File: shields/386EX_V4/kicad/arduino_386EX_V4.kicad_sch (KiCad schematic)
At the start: 48 parts, among them J1 Conn_01x02_Pin, J2 JTAG, J3 Conn_01x04_Pin, J4 Conn_01x04_Pin, J5 Conn_01x04_Pin, J6 SERIAL0, J9 WP Jumper, U1 AT24CS01-STUM, U11 I386EX_PQFP, U2 ULN2003A, U3 SN74LV14A

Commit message: Fixed oversight of I2C SDA and SCK pull-up resistors; rearranged EEPROM IC to accommodate.
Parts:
- added R14, R15: 3.3 K Ohm, Resistor_SMD:R_0603_1608Metric_Pad0.98x0.95mm_HandSolder, symbol Device:R
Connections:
- net +3.3VP: now also R14.2, R15.2
- net SCL: now also R15.1
- net SDA: now also R14.1
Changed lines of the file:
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@@
 	)
 	(junction
+		(at 300.99 143.51)
+		(diameter 0)
+		(color 0 0 0 0)
+	)
+	(junction
 		(at 386.08 45.72)
 		(diameter 0)
@@
 	)
 	(junction
+		(at 304.8 143.51)
+		(diameter 0)
+		(color 0 0 0 0)
+	)
+	(junction
 		(at 320.04 177.8)
 		(diameter 0)
@@
 	)
 	(junction
+		(at 304.8 158.75)
+		(diameter 0)
+		(color 0 0 0 0)
+	)
+	(junction
 		(at 257.81 256.54)
 		(diameter 0)
@@
 	)
 	(junction
+		(at 300.99 156.21)
+		(diameter 0)
+		(color 0 0 0 0)
+	)
+	(junction
 		(at 257.81 259.08)
 		(diameter 0)
@@
 	(wire
 		(pts
+			(xy 304.8 143.51) (xy 304.8 146.05)
+		)
+		(stroke
+			(width 0)
+			(type default)
+		)
+	)
+	(wire
+		(pts
 			(xy 201.93 287.02) (xy 201.93 294.64)
 		)
@@
 	(wire
 		(pts
-			(xy 287.02 143.51) (xy 320.04 143.51)
+			(xy 287.02 143.51) (xy 300.99 143.51)
 		)
 		(stroke
@@
 	(wire
 		(pts
+			(xy 304.8 153.67) (xy 304.8 158.75)
+		)
+		(stroke
+			(width 0)
+			(type default)
+		)
+	)
+	(wire
+		(pts
 			(xy 95.25 68.58) (xy 100.33 68.58)
 		)
@@
 	(wire
 		(pts
+			(xy 304.8 143.51) (xy 320.04 143.51)
+		)
+		(stroke
+			(width 0)
+			(type default)
+		)
+	)
+	(wire
+		(pts
 			(xy 63.5 233.68) (xy 63.5 241.3)
 		)
@@
 	(wire
 		(pts
+			(xy 300.99 153.67) (xy 300.99 156.21)
+		)
+		(stroke
+			(width 0)
+			(type default)
+		)
+	)
+	(wire
+		(pts
 			(xy 317.5 165.1) (xy 317.5 161.29)
 		)
@@
 	(wire
 		(pts
+			(xy 300.99 143.51) (xy 304.8 143.51)
+		)
+		(stroke
+			(width 0)
+			(type default)
+		)
+	)
+	(wire
+		(pts
 			(xy 100.33 119.38) (xy 95.25 119.38)
 		)
@@
 	(wire
 		(pts
+			(xy 300.99 156.21) (xy 336.55 156.21)
+		)
+		(stroke
+			(width 0)
+			(type default)
+		)
+	)
+	(wire
+		(pts
 			(xy 50.8 323.85) (xy 50.8 332.74)
 		)
@@
 	(wire
 		(pts
-			(xy 297.18 156.21) (xy 336.55 156.21)
+			(xy 297.18 156.21) (xy 300.99 156.21)
 		)
 		(stroke
@@
 	(wire
 		(pts
-			(xy 297.18 158.75) (xy 336.55 158.75)
+			(xy 297.18 158.75) (xy 304.8 158.75)
 		)
 		(stroke
@@
 	(wire
 		(pts
+			(xy 300.99 143.51) (xy 300.99 146.05)
+		)
+		(stroke
+			(width 0)
+			(type default)
+		)
+	)
+	(wire
+		(pts
 			(xy 95.25 214.63) (xy 95.25 220.98)
 		)
@@
 	(wire
 		(pts
+			(xy 304.8 158.75) (xy 336.55 158.75)
+		)
+		(stroke
+			(width 0)
+			(type default)
+		)
+	)
+	(wire
+		(pts
 			(xy 346.71 40.64) (xy 356.87 40.64)
 		)
@@
 	)
 	(symbol
+		(lib_id "Device:R")
+		(at 304.8 149.86 180)
+		(unit 1)
+		(exclude_from_sim no)
+		(in_bom yes)
+		(on_board yes)
+		(dnp no)
+		(property "Reference" "R15"
+			(at 307.34 148.5899 0)
+			(effects
+				(font
+					(size 1.27 1.27)
+				)
+				(justify right)
+			)
+		)
+		(property "Value" "3.3 K Ohm"
+			(at 307.34 151.1299 0)
+			(effects
+				(font
+					(size 1.27 1.27)
+				)
+				(justify right)
+			)
+		)
+		(property "Footprint" "Resistor_SMD:R_0603_1608Metric_Pad0.98x0.95mm_HandSolder"
+			(at 306.578 149.86 90)
+			(effects
+				(font
+					(size 1.27 1.27)
+				)
+				(hide yes)
+			)
+		)
+		(property "Datasheet" "~"
+			(at 304.8 149.86 0)
+			(effects
+				(font
+					(size 1.27 1.27)
+				)
+				(hide yes)
+			)
+		)
+		(property "Description" "Resistor"
+			(at 304.8 149.86 0)
+			(effects
+				(font
+					(size 1.27 1.27)
+				)
+				(hide yes)
+			)
+		)
+		(pin "2"
+		)
+		(pin "1"
+		)
+		(instances
+			(project "arduino_386EX_V4"
+				(path "/2ed64d3c-1ac9-4d9f-9649-2011440e90de"
+					(reference "R15")
+					(unit 1)
+				)
+			)
+		)
+	)
+	(symbol
 		(lib_id "mega:Arduino_Mega2560_Shield")
 		(at 133.35 102.87 0)
@@
 					(unit 1)
 				)
+			)
+		)
+	)
+	(symbol
+		(lib_id "Device:R")
+		(at 300.99 149.86 0)
+		(mirror x)
+		(unit 1)
+		(exclude_from_sim no)
+		(in_bom yes)
+		(on_board yes)
+		(dnp no)
+		(property "Reference" "R14"
+			(at 298.45 148.5899 0)
+			(effects
+				(font
+					(size 1.27 1.27)
+				)
+				(justify right)
+			)
+		)
+		(property "Value" "3.3 K Ohm"
+			(at 298.45 151.1299 0)
+			(effects
+				(font
+					(size 1.27 1.27)
+				)
+				(justify right)
+			)
+		)
+		(property "Footprint" "Resistor_SMD:R_0603_1608Metric_Pad0.98x0.95mm_HandSolder"
+			(at 299.212 149.86 90)
+			(effects
+				(font
+					(size 1.27 1.27)
+				)
+				(hide yes)
+			)
+		)
+		(property "Datasheet" "~"
+			(at 300.99 149.86 0)
+			(effects
+				(font
+					(size 1.27 1.27)
+				)
+				(hide yes)
+			)
+		)
+		(property "Description" "Resistor"
+			(at 300.99 149.86 0)
+			(effects
+				(font
+					(size 1.27 1.27)
+				)
+				(hide yes)
+			)
+		)
+		(pin "2"
+		)
+		(pin "1"
+		)
+		(instances
+			(project "arduino_386EX_V4"
+				(path "/2ed64d3c-1ac9-4d9f-9649-2011440e90de"
+					(reference "R14")
+					(unit 1)
+				)

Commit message: Added 2x 1N4148 diodes for combining 3.3V off-board supplies, updated HTML BOM.
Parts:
- added D3, D9: 1N4148, Diode_THT:D_DO-35_SOD27_P7.62mm_Horizontal, symbol Diode:1N4148
- C5: renamed from C3; footprint (none) -> Capacitor_SMD:C_0603_1608Metric_Pad1.08x0.95mm_HandSolder
- renumbered C14 to C1, C6 to C11, C9 to C12, C8 to C13, C7 to C14, C13 to C2, C1 to C3, C2 to C4, C12 to C6, C4 to C7, C11 to C8, C5 to C9, D3 to D4, D4 to D5, D5 to D6, D6 to D7, D7 to D8, J9 to J1, J1 to J2, J5 to J3, J6 to J4, J4 to J5, J3 to J6, J2 to J7, R12 to R1, R6 to R10, R7 to R11, R13 to R12, R8 to R13, R9 to R14, R10 to R15, R1 to R2, R2 to R3, R3 to R4, R4 to R5, R14 to R6, R15 to R7, R11 to R8, R5 to R9, T_CLK2_GND1 to T_CLK1, U2 to U1, U3 to U2, U1 to U3, U11 to U4
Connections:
- net +3.3V: now also D3.2 (A)
- net +3.3VP: now also D9.2 (A); no longer J6.1 (Pin_1), R6.2, R7.2, R8.2, U3.4 (VCC)
- new net 3.3V_COMBINED: D3.1 (K), D9.1 (K), J6.1 (Pin_1), R6.2, R7.2, R8.2, U3.4 (VCC)
- no-connect marks 13 -> 19
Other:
- moved on the sheet: J6

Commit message: Updated 386EX to rev 5.1; added LDL1117 LDO, swapped to SMD diodes, tidied schematic.
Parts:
- removed C1: C_Polarized, Capacitor_THT:C_Disc_D5.0mm_W2.5mm_P2.50mm, symbol Device:C_Polarized
- removed C2: C_Polarized, Capacitor_THT:C_Radial_D4.0mm_H5.0mm_P1.50mm, symbol Device:C_Polarized
- removed D3, D9: 1N4148, Diode_THT:D_DO-35_SOD27_P7.62mm_Horizontal, symbol Diode:1N4148
- added C1: 4.7 uF, Capacitor_SMD:C_0805_2012Metric, symbol Device:C_Small
- added C2: 1 uF, Capacitor_SMD:C_0805_2012Metric, symbol Device:C_Small
- added D10, D3, D9: S1A-13-F, Diodes Inc S1A-13-F 50V 1A standard diode:DIOM5226X240N, symbol S1A-13-F:S1A-13-F
- added J3: WP Jumper, Connector_PinHeader_2.54mm:PinHeader_1x03_P2.54mm_Vertical, symbol Connector:Conn_01x03_Pin
- added U1: LDL1117S33R, ST LDL1117S33R 1A 3.3V LDO:SOT223_STM-M, symbol LDL1117S33R:LDL1117S33R
- J2: footprint Connector_PinHeader_2.54mm:PinHeader_1x02_P2.54mm_Horizontal -> Connector_PinHeader_2.54mm:PinHeader_1x02_P2.54mm_Vertical
- renumbered T_CLK1 to GND, J3 to J5, J5 to J6, J6 to J7, J7 to J8, T_CLK2 to T_CLK1, U1 to U2, U2 to U3, U3 to U4, U4 to U5
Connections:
- net GND: now also C1.2, C2.2, U1.1 (GND)
- net ARDUINO_5V: now reaches XA1.5V1 (5V)
- net ARDUINO_5V: now also XA1.5V3 (5V), XA1.5V4 (5V), J3.3 (Pin_3)
- net +3.3V renamed ARDUINO_3.3V
- net +3.3VP renamed 3.3V_LOCAL
- net 3.3V_LOCAL: now also R6.2, R7.2, R8.2, U4.4 (VCC), C1.1, D10.1 (K), D9.2 (A), U1.2 (VOUT), U1.4 (VOUT); no longer J2.1 (Pin_1), J8.5 (Pin_5)
- removed net 3.3V_COMBINED: J7.1 (Pin_1), R6.2, R7.2, R8.2, U4.4 (VCC)
- new net: D3.2 (A), J2.1 (Pin_1)
- new net: D9.1 (K), J7.1 (Pin_1)
- new net: D10.2 (A), J8.5 (Pin_5)
- new net EXT_5V: D3.1 (K), J3.1 (Pin_1)
- new net PWR_SELECTED: C2.1, J3.2 (Pin_2), U1.3 (VIN)
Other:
- note added: "3.3V 1.2A LDO"
- note added: "386EX CPU (PQFP-132)"
- note added: "Blinkenlights (Status LEDs)"
- note added: "External 5V Power Connector"
- note added: "HAT ID EEPROM"
- note added: "JTAG Header (3.3V power in only)"
- note added: "Power source selection header"
- note removed: "386EX (PQFP-132)"
- note removed: "Blinkenlights"
- note removed: "External Power Connector"
- note removed: "ID EEPROM"
- note removed: "JTAG Header"
- moved on the sheet: C10, C11, C12, C13, C14, C3, C4, C5, C6, C7, C8, C9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

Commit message: Reverted 386EX_V4 to track with original fork of repo.
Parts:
- removed C1: 4.7 uF, Capacitor_SMD:C_0805_2012Metric, symbol Device:C_Small
- removed C10, C11, C12, C13, C14, C3, C4, C5, C6, C7, C8, C9: 0.1 uF, Capacitor_SMD:C_0603_1608Metric_Pad1.08x0.95mm_HandSolder, symbol Device:C_Small
- removed C2: 1 uF, Capacitor_SMD:C_0805_2012Metric, symbol Device:C_Small
- removed D10, D3, D9: S1A-13-F, Diodes Inc S1A-13-F 50V 1A standard diode:DIOM5226X240N, symbol S1A-13-F:S1A-13-F
- removed J3: WP Jumper, Connector_PinHeader_2.54mm:PinHeader_1x03_P2.54mm_Vertical, symbol Connector:Conn_01x03_Pin
- removed R12, R14, R6, R7: 3.3 K Ohm, Resistor_SMD:R_0603_1608Metric_Pad0.98x0.95mm_HandSolder, symbol Device:R
- removed U1: LDL1117S33R, ST LDL1117S33R 1A 3.3V LDO:SOT223_STM-M, symbol LDL1117S33R:LDL1117S33R
- removed unit 6 of U3
- removed unit 5 of U3
- added C1, C10, C11, C12, C2, C3, C4, C5, C6, C7, C8, C9: C, Capacitor_SMD:C_0603_1608Metric_Pad1.08x0.95mm_HandSolder, symbol Device:C
- added C13: C_Polarized, Capacitor_THT:C_Radial_D4.0mm_H5.0mm_P1.50mm, symbol Device:C_Polarized
- added C14: C_Polarized, Capacitor_THT:C_Disc_D5.0mm_W2.5mm_P2.50mm, symbol Device:C_Polarized
- J1: renamed from J2; footprint Connector_PinHeader_2.54mm:PinHeader_1x02_P2.54mm_Vertical -> Connector_PinHeader_2.54mm:PinHeader_1x02_P2.54mm_Horizontal
- R11: renamed from R8; value 3.3 K Ohm -> R
- R12: renamed from R1; value 3.3 K Ohm -> R
- renumbered D4 to D3, D5 to D4, D6 to D5, D7 to D6, D8 to D7, J8 to J2, J7 to J3, J6 to J4, J4 to J6, J1 to J9, R2 to R1, R15 to R10, R3 to R2, R4 to R3, R5 to R4, R9 to R5, R10 to R6, R11 to R7, R13 to R8, T_CLK1 to T_CLK2, GND to T_CLK2_GND1, U4 to U1, U5 to U11
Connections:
- net 3.3V_LOCAL is gone; now on net +3.3VP: D1.2 (A), D2.2 (A), D3.2 (A), D4.2 (A), D5.2 (A), D6.2 (A), D7.2 (A), R11.2, U1.4 (VCC), U11.109 (VCC), U11.121 (VCC), U11.127 (VCC), U11.15 (VCC), U11.28 (VCC), U11.38 (VCC), U11.47 (VCC), U11.60 (VCC), U11.71 (VCC), U11.81 (VCC), U11.88 (VCC), U11.9 (VCC), U2.9 (COM), U3.14 (VCC)
- net GND: now also C1.1, C10.1, C11.1, C12.1, C13.2, C14.2, C2.1, C3.1, C4.1, C5.1, C6.1, C7.1, C8.1, C9.1
- net RD: now also U3.10
- net WR: now also U3.12
- net ~{RD}: now also U3.11
- net ~{WR}: now also U3.13
- net +3.3VP: now reaches J1.1 (Pin_1)
- net +3.3VP: now also J2.5 (Pin_5), J3.1 (Pin_1), C1.2, C10.2, C11.2, C12.2, C13.1, C14.1, C2.2, C3.2, C4.2, C5.2, C6.2, C7.2, C8.2, C9.2
- net ARDUINO_3.3V renamed +3.3V
- removed net ARDUINO_5V: XA1.5V1 (5V), XA1.5V3 (5V), XA1.5V4 (5V)
- no-connect marks 19 -> 13
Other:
- note added: "386EX (PQFP-132)"
- note added: "Blinkenlights"
- note added: "External Power Connector"
- note added: "ID EEPROM"
- note added: "JTAG Header"
- note removed: "3.3V 1.2A LDO"
- note removed: "386EX CPU (PQFP-132)"
- note removed: "Blinkenlights (Status LEDs)"
- note removed: "External 5V Power Connector"
- note removed: "HAT ID EEPROM"
- note removed: "JTAG Header (3.3V power in only)"
- note removed: "Power source selection header"
- moved on the sheet: D1, D2, D3, D4, D5, D6, D7, J1, J2, J3, J4, J5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

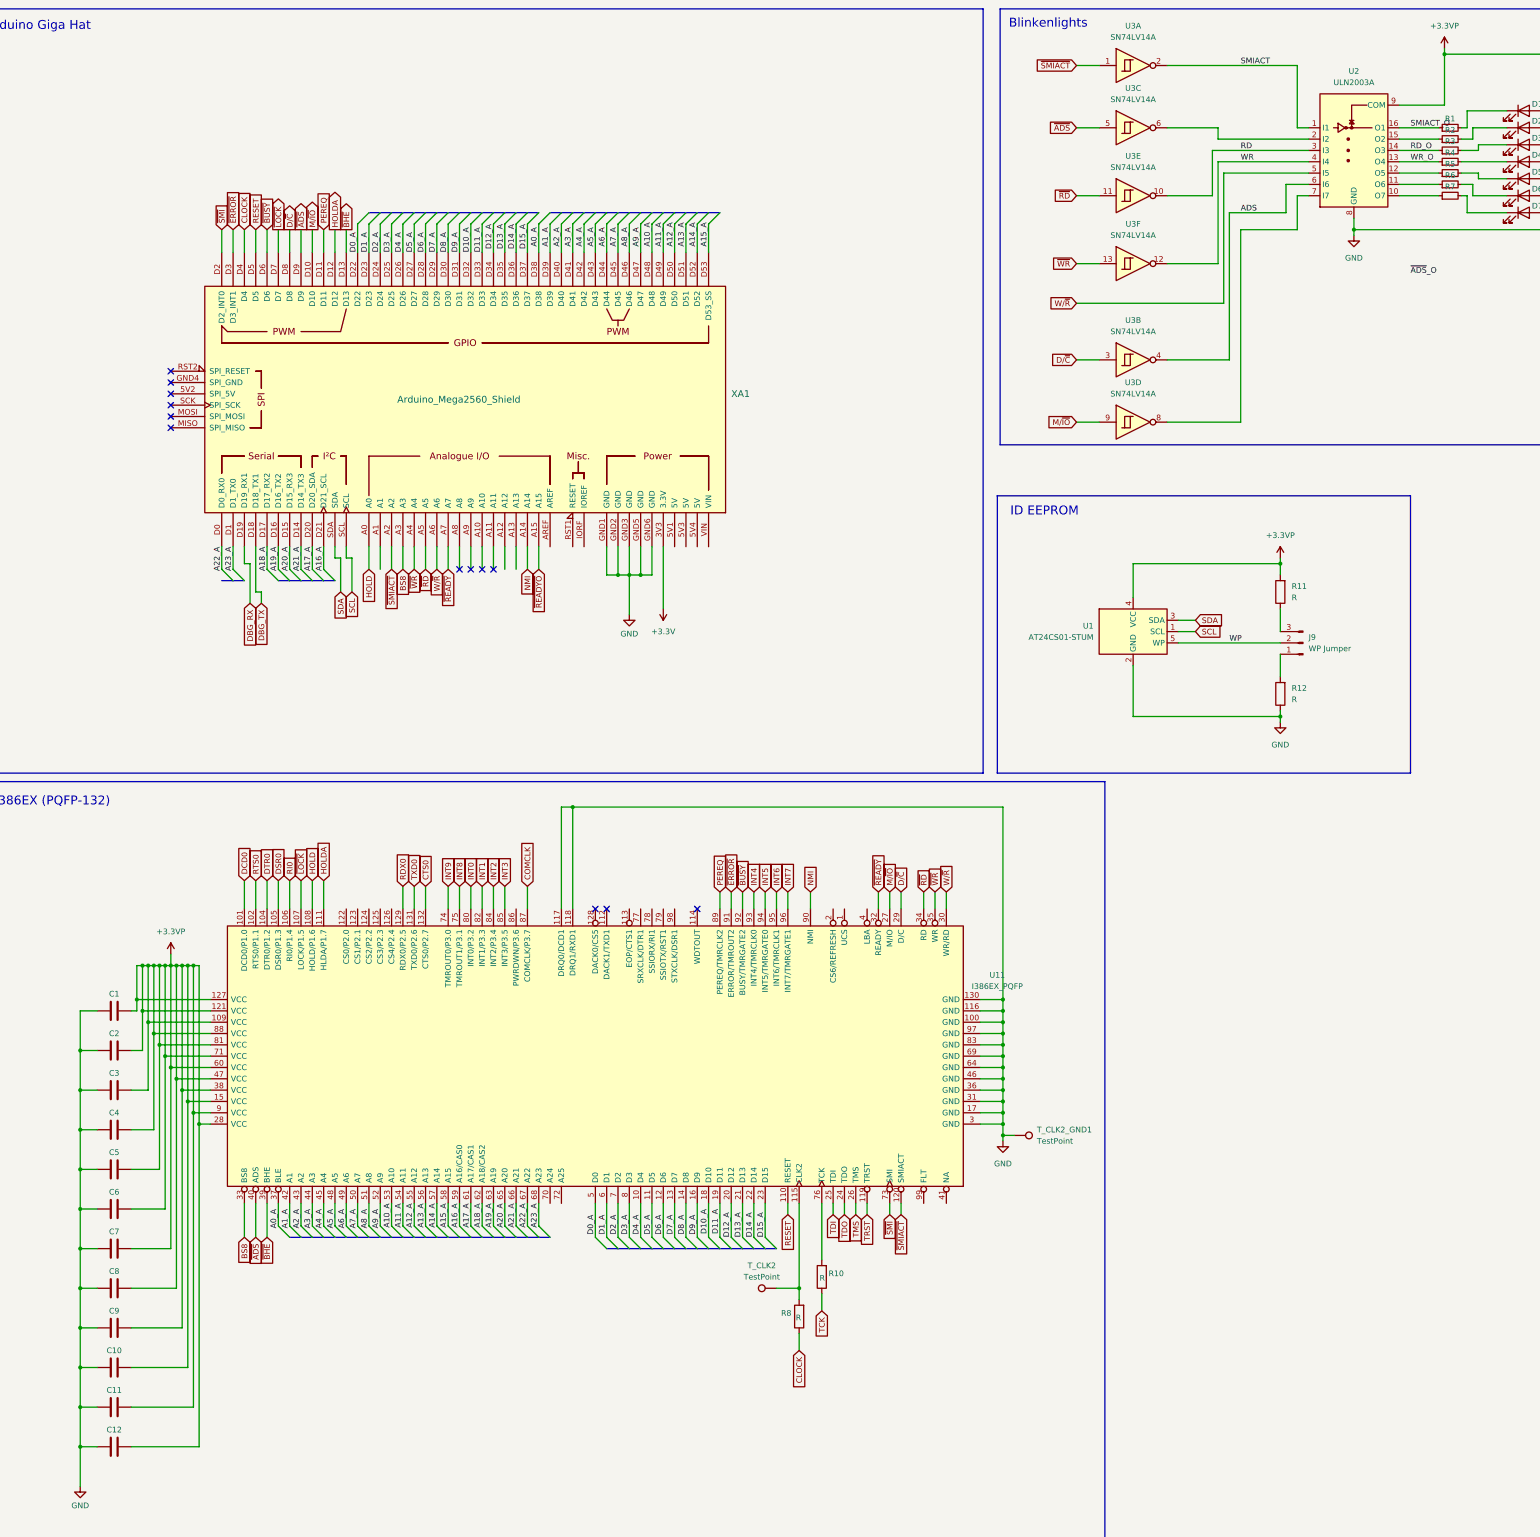
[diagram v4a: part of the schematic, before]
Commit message: Added I2C SDA, SCK, ~ERROR and ~LOCK pull-up resistors; resolved minor DRC errors.
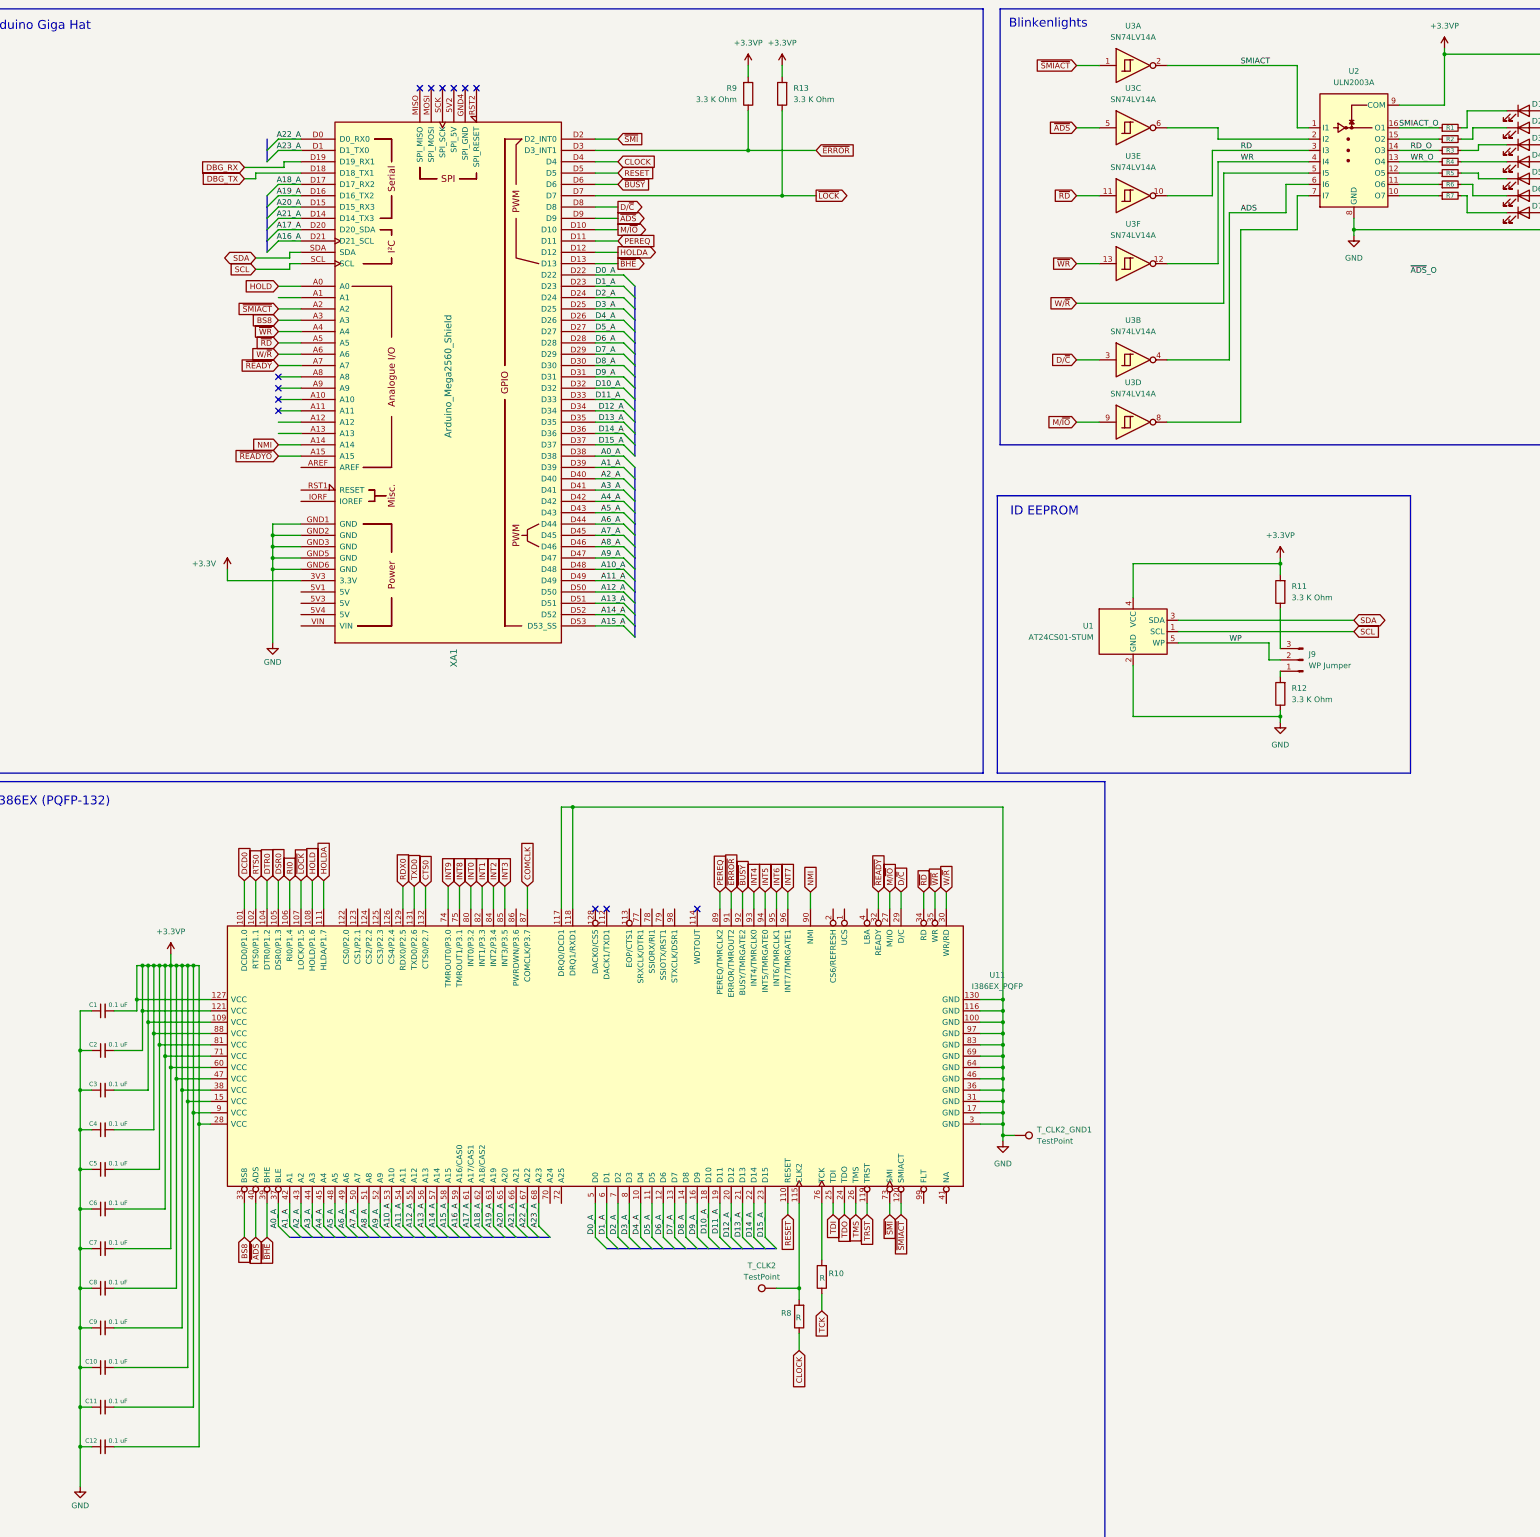
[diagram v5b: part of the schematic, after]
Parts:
- removed C1, C10, C11, C12, C2, C3, C4, C5, C6, C7, C8, C9: C, Capacitor_SMD:C_0603_1608Metric_Pad1.08x0.95mm_HandSolder, symbol Device:C
- added C1, C10, C11, C12, C2, C4, C5, C6, C7, C8, C9: 0.1 uF, Capacitor_SMD:C_0603_1608Metric_Pad1.08x0.95mm_HandSolder, symbol Device:C_Small
- added C3: 0.1 uF, symbol Device:C_Small
- added R13, R9: 3.3 K Ohm, Resistor_SMD:R_0603_1608Metric_Pad0.98x0.95mm_HandSolder, symbol Device:R
- added unit 6 of U3
- added unit 5 of U3
- R11, R12: value R -> 3.3 K Ohm
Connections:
- net +3.3VP: now also C1.2, C10.2, C11.2, C12.2, C2.2, C3.2, C4.2, C5.2, C6.2, C7.2, C8.2, C9.2, R13.2, R9.2
- net GND: now also C1.1, C10.1, C11.1, C12.1, C2.1, C3.1, C4.1, C5.1, C6.1, C7.1, C8.1, C9.1
- net RD: now also U3.10; no longer U3.10
- net WR: now also U3.12; no longer U3.12
- net ~{ERROR}: now also R9.1
- net ~{LOCK}: now also R13.1
- net ~{RD}: now also U3.11; no longer U3.11
- net ~{WR}: now also U3.13; no longer U3.13
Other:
- moved on the sheet: J9, XA1
